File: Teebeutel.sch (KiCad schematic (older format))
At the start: 71 parts, among them J1 RJ45_Shielded, J2 Conn_01x30_Female, J3 Micro_SD_Card, Q1 S8050, Q2 S8050, Q3 S8050, SW1 K1-1506SN-01, U1 ESP32-WROOM-32, U2 TLV1117-33, U3 MCP73831-2-OT, U4 SDB628, U5 LIS2DE12, U6 TLV70018_SOT23-5, U7 SGP30, U8 PPSI262, U9 TXB0104RUT

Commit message: feat: alot of stuff and routing
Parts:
- added C1, C12, C2, C3, C4: 100n, Capacitor_SMD:C_0603_1608Metric, symbol Device:C
- added J3: Battery, Connector_PinHeader_2.54mm:PinHeader_1x02_P2.54mm_Vertical, symbol Connector_Generic:Conn_01x02
- added R20: 30k, Resistor_SMD:R_0603_1608Metric, symbol Device:R
- added R21: 100k, Resistor_SMD:R_0603_1608Metric, symbol Device:R
- added SW2: SW_SPST, Button_Switch_SMD:SW_SPDT_PCM12, symbol Switch:SW_SPDT
- added TP1: ESP32 EN, TestPoint:TestPoint_Pad_D1.0mm, symbol Connector:TestPoint
- added TP10: DTR 3.3V, TestPoint:TestPoint_Pad_D1.0mm, symbol Connector:TestPoint
- added TP11: TxD 3.3V, TestPoint:TestPoint_Pad_D1.0mm, symbol Connector:TestPoint
- added TP12: RxD 3.3V, TestPoint:TestPoint_Pad_D1.0mm, symbol Connector:TestPoint
- added TP13: RTS 3.3V, TestPoint:TestPoint_Pad_D1.0mm, symbol Connector:TestPoint
- added TP14: I²C SDA, TestPoint:TestPoint_Pad_D1.0mm, symbol Connector:TestPoint
- added TP15: I²C SCL, TestPoint:TestPoint_Pad_D1.0mm, symbol Connector:TestPoint
- added TP16, TP17: TestPoint, TestPoint:TestPoint_Pad_D1.0mm, symbol Connector:TestPoint
- added TP18: SD-Card CS, TestPoint:TestPoint_Pad_D1.0mm, symbol Connector:TestPoint
- added TP19: SD-Card MISO, TestPoint:TestPoint_Pad_D1.0mm, symbol Connector:TestPoint
- added TP2: WS2821, TestPoint:TestPoint_Pad_D1.0mm, symbol Connector:TestPoint
- added TP20: SD-Card MOSI, TestPoint:TestPoint_Pad_D1.0mm, symbol Connector:TestPoint
- added TP21: SD-Card SCK, TestPoint:TestPoint_Pad_D1.0mm, symbol Connector:TestPoint
- added TP22: V +5V, TestPoint:TestPoint_Pad_D1.0mm, symbol Connector:TestPoint
- added TP23: V Battery, TestPoint:TestPoint_Pad_D1.0mm, symbol Connector:TestPoint
- added TP24: Charging status, TestPoint:TestPoint_Pad_D1.0mm, symbol Connector:TestPoint
- added TP25: ADC Battery (1/4 Battery voltage), TestPoint:TestPoint_Pad_D1.0mm, symbol Connector:TestPoint
- added TP26: V +1.8V, TestPoint:TestPoint_Pad_D1.0mm, symbol Connector:TestPoint
- added TP27: OLED VPP (13V), TestPoint:TestPoint_Pad_D1.0mm, symbol Connector:TestPoint
- added TP28: OLED SDA, TestPoint:TestPoint_Pad_D1.0mm, symbol Connector:TestPoint
- added TP29: OLED SCK, TestPoint:TestPoint_Pad_D1.0mm, symbol Connector:TestPoint
- added TP3: Button Down, TestPoint:TestPoint_Pad_D1.0mm, symbol Connector:TestPoint
- added TP30: OLED CS, TestPoint:TestPoint_Pad_D1.0mm, symbol Connector:TestPoint
- added TP31: OLED DC, TestPoint:TestPoint_Pad_D1.0mm, symbol Connector:TestPoint
- added TP32: OLED RESET, TestPoint:TestPoint_Pad_D1.0mm, symbol Connector:TestPoint
- added TP33: Touch Button 1, Symbol:OSHW-Symbol_13.4x12mm_Copper, symbol Connector:TestPoint
- added TP34: Touch Button 2, Symbol:OSHW-Symbol_13.4x12mm_Copper, symbol Connector:TestPoint
- added TP35: V +3.3V, TestPoint:TestPoint_Pad_D1.0mm, symbol Connector:TestPoint
- added TP4: Button Left, TestPoint:TestPoint_Pad_D1.0mm, symbol Connector:TestPoint
- added TP5: Button Up, TestPoint:TestPoint_Pad_D1.0mm, symbol Connector:TestPoint
- added TP6: ESP32 IO0, TestPoint:TestPoint_Pad_D1.0mm, symbol Connector:TestPoint
- added TP7: Button Push, TestPoint:TestPoint_Pad_D1.0mm, symbol Connector:TestPoint
- added TP8: Button Right, TestPoint:TestPoint_Pad_D1.0mm, symbol Connector:TestPoint
- added TP9: Buzzer, TestPoint:TestPoint_Pad_D1.0mm, symbol Connector:TestPoint
- BZ1: footprint (none) -> custom_parts:KLJ-5020
- Q1, Q2, Q3: footprint Package_TO_SOT_THT:TO-92_Inline -> Package_TO_SOT_SMD:SOT-23; symbol Transistor_BJT:S8050 -> custom-parts:S8050-J3Y
- gave numbers to parts that had none: 1
- renumbered C2 to C10, C4 to C11, C5 to C13, C6 to C14, C7 to C15, C8 to C16, C9 to C17, C10 to C18, C14 to C19, C3 to C20, C15 to C21, C16 to C22, C11 to C23, C17 to C24, C18 to C5, C19 to C6, C12 to C7, C13 to C8, C1 to C9, D4 to D1, D3 to D10, D7 to D2, D8 to D3, D9 to D4, D10 to D5, D5 to D6, D6 to D7, D1 to D8, D2 to D9, J3 to J2, J2 to J4, R18 to R10, R23 to R11, R8 to R12, R19 to R13, R16 to R14, R20 to R15, R3 to R16, R9 to R18, R10 to R19, R4 to R22, R7 to R23, R5 to R24, R6 to R25, R11 to R3, R12 to R4, R13 to R5, R21 to R6, R22 to R7, R14 to R8, R15 to R9, U2 to U10, U9 to U3, U5 to U4, U7 to U5, U8 to U6, U3 to U7, U6 to U8, U4 to U9
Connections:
- net labels added: ADC-BAT
- wire segments 238 -> 294
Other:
- moved on the sheet: C10, C11, C13, C14, C15, C16, C17, C18, C19, C20, C21, C22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

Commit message: feat: alot of stuff
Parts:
- removed BZ1: Buzzer, custom_parts:KLJ-5020, symbol Device:Buzzer
- removed D2, D3, D4: WS2812B, LED_SMD:LED_WS2812B_PLCC4_5.0x5.0mm_P3.2mm, symbol LED:WS2812B
- removed D5: SM4007, Diode_SMD:D_SOD-123, symbol Diode:SM4007
- removed Q3: S8050, Package_TO_SOT_SMD:SOT-23, symbol custom-parts:S8050-J3Y
- removed TP22: V +5V, TestPoint:TestPoint_Pad_D1.0mm, symbol Connector:TestPoint
- removed TP23: V Battery, TestPoint:TestPoint_Pad_D1.0mm, symbol Connector:TestPoint
- removed TP33: Touch Button 1, Symbol:OSHW-Symbol_13.4x12mm_Copper, symbol Connector:TestPoint
- removed TP9: Buzzer, TestPoint:TestPoint_Pad_D1.0mm, symbol Connector:TestPoint
- added C1, C11, C12, C13, C14, C4, C7, C9: 100n, Capacitor_SMD:C_0603_1608Metric, symbol Device:C
- added D1, D10, D11, D12, D3, D4, D5, D6, D7, D8, D9: WS2812B, Teebeutel_Special_Parts:WS2812B-4020, symbol Teebeutel_Special_Parts:WS2812B-4020
- added TB1: Touch Button 2, Teebeutel_Graphics:Touch-Button_Python, symbol Connector:TestPoint
- D13: renamed from D6; value LED -> LED-RED
- D14: renamed from D7; value LED -> LED-GREEN
- D2: renamed from D1; footprint LED_SMD:LED_WS2812B_PLCC4_5.0x5.0mm_P3.2mm -> Teebeutel_Special_Parts:WS2812B-4020; symbol LED:WS2812B -> Teebeutel_Special_Parts:WS2812B-4020; JLCPCB C139127 -> C965557
- J2: footprint custom_parts:TF15X15 -> Teebeutel_Special_Parts:TF15X15
- Q1, Q2: symbol custom-parts:S8050-J3Y -> Teebeutel_Special_Parts:S8050-J3Y
- R11: value 180 -> 10k
- R20: value 30k -> 300k
- SW1: footprint custom_parts:K1-1506SN-01 -> Teebeutel_Special_Parts:K1-1506SN-01; symbol custom-parts:K1-1506SN-01 -> Teebeutel_Special_Parts:K1-1506SN-01
- TB2: renamed from TP34; footprint Symbol:OSHW-Symbol_13.4x12mm_Copper -> Teebeutel_Graphics:Touch-Button_OSHW
- U5: footprint custom_parts:SGP30 -> Teebeutel_Special_Parts:SGP30; symbol custom-parts:SGP30 -> Teebeutel_Special_Parts:SGP30
- U6: footprint custom_parts:PPSI262 -> Teebeutel_Special_Parts:PPSI262; symbol custom-parts:PPSI262 -> Teebeutel_Special_Parts:PPSI262
- U9: symbol custom-parts:SDB628 -> Teebeutel_Special_Parts:SDB628
- renumbered C4 to C10, C5 to C15, C6 to C16, C9 to C17, C10 to C18, C11 to C19, C1 to C2, C12 to C20, C13 to C21, C14 to C22, C15 to C23, C16 to C24, C17 to C25, C18 to C26, C19 to C27, C20 to C28, C21 to C29, C7 to C3, C22 to C30, C23 to C31, C24 to C32, C2 to C5, C8 to C6, C3 to C8, D8 to D15, D9 to D16, D10 to D17, R12 to R1, R8 to R10, R9 to R12, R1 to R2, R2 to R3, R6 to R4, R7 to R5, R3 to R6, R10 to R7, R4 to R8, R5 to R9, TP12 to TP10, TP13 to TP11, TP8 to TP12, TP14 to TP13, TP15 to TP14, TP16 to TP15, TP17 to TP16, TP18 to TP17, TP19 to TP18, TP20 to TP19, TP21 to TP20, TP24 to TP21, TP25 to TP22, TP26 to TP23, TP27 to TP24, TP28 to TP25, TP29 to TP26, TP30 to TP27, TP31 to TP28, TP32 to TP29, TP6 to TP3, TP35 to TP30, TP3 to TP4, TP4 to TP5, TP5 to TP6, TP10 to TP8, TP11 to TP9, U4 to U1, U1 to U2, U2 to U3, U3 to U4
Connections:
- net labels removed: BUZZER
- wire segments 294 -> 315
- no-connect marks 23 -> 29
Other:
- moved on the sheet: C10, C2, C3, C5, C6, C8, R1, R10, R12, R6, R8, R9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

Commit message: feat(): Finished routing and some clean up
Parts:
- added R26: 10, Resistor_SMD:R_0603_1608Metric, symbol Device:R
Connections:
- net SD-SCK: now also R26.2; no longer J2.5 (CLK), TP20.1
- new net: J2.5 (CLK), R26.1, TP20.1
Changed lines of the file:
@@
 Text GLabel 8750 1650 0    50   Input ~ 0
 SD-MISO
-Text GLabel 8750 1250 0    50   Input ~ 0
+Text GLabel 8450 1250 1    50   Input ~ 0
 SD-MOSI
-Text GLabel 8750 1150 0    50   Input ~ 0
-SD-CS
-Text GLabel 8750 1450 0    50   Input ~ 0
+Text GLabel 8450 1450 0    50   Input ~ 0
 SD-SCK
 $Comp
@@
 Wire Wire Line
 	8750 1150 9000 1150
-Wire Wire Line
-	8750 1250 8950 1250
 $Comp
 L Connector:TestPoint TP19
@@
 NoConn ~ 7000 10500
 NoConn ~ 12000 7250
+$Comp
+L Device:R R26
+U 1 1 6238B3D1
+P 8600 1450
+F 0 "R26" H 8530 1404 50  0000 R CNN
+F 1 "10" H 8530 1495 50  0000 R CNN
+F 2 "Resistor_SMD:R_0603_1608Metric" V 8530 1450 50  0001 C CNN
+F 3 "~" H 8600 1450 50  0001 C CNN
+	1    8600 1450
+	0    1    1    0
+$EndComp
+Text GLabel 8600 1150 1    50   Input ~ 0
+SD-CS
+Wire Wire Line
+	8600 1150 8750 1150
+Connection ~ 8750 1150
+Wire Wire Line
+	8450 1250 8950 1250
 $EndSCHEMATC

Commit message: feat(): finish routing and assigning JLCPCB part numbers
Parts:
- added R27, R28: 100, Resistor_SMD:R_0603_1608Metric, symbol Device:R
- C1, C10, C11, C12, C13, C14, C15, C16, C2, C20, C24, C27, C3, C30, C4, C5, C7, C8, C9: JLC (none) -> 0603; LCSC (none) -> C14663
- C17, C18, C21, C23, C29, C32, C6: JLC (none) -> 0603; LCSC (none) -> C19702
- C19, C22: JLC (none) -> 0603; LCSC (none) -> C15849
- C25, C26: JLC (none) -> 0603; LCSC (none) -> C19666
- C28, C31: JLC (none) -> 0603; LCSC (none) -> C59461
- D1, D10, D11, D12, D2, D3, D4, D5, D6, D7, D8, D9: JLC (none) -> 4.0x2.0mm; JLCPCB C965557 -> (none); LCSC (none) -> C965557
- D13: footprint LED_SMD:LED_1210_3225Metric -> LED_SMD:LED_0805_2012Metric; JLC (none) -> LED_0805; LCSC (none) -> C84256
- D14: footprint LED_SMD:LED_1210_3225Metric -> LED_SMD:LED_0805_2012Metric; JLC (none) -> LED_0805; LCSC (none) -> C2297
- D15, D16: JLC (none) -> SOD-523; LCSC (none) -> C393518
- D17: JLC (none) -> DO-214AC; JLCPCB C2480 -> (none); LCSC (none) -> C2480
- J1: footprint Connector_RJ:RJ45_Amphenol_RJHSE5380 -> Connector_RJ:RJ45_Amphenol_RJHSE538X; symbol Connector:RJ45_Shielded -> Connector:RJ45_LED_Shielded; JLC (none) -> RJ45-TH; LCSC (none) -> C464587
- J2: JLC (none) -> 14.5x14.75x1.85mm; JLCPCB C266621 -> (none); LCSC (none) -> C266621
- J4: JLC (none) -> SMD; JLCPCB C2856808 -> (none); LCSC (none) -> C2856808
- L1: JLC (none) -> 1210; JLCPCB C86070 -> (none); LCSC (none) -> C86070
- Q1, Q2: JLC (none) -> SOT-23-3; JLCPCB C2146 -> (none); LCSC (none) -> C2146
- R1, R10, R11, R12, R13, R14, R15, R17, R2, R3, R4, R5, R6, R7, R8, R9: JLC (none) -> 0603; LCSC (none) -> C25804
- R16: JLC (none) -> R0603; LCSC (none) -> C113303
- R18, R19: JLC (none) -> R0603; LCSC (none) -> C116694
- R20: JLC (none) -> 0603; LCSC (none) -> C23024
- R21: JLC (none) -> 0603; LCSC (none) -> C25803
- R22: value 50 -> 56; JLC (none) -> 0603; LCSC (none) -> C25196
- R23: JLC (none) -> 0603; LCSC (none) -> C23203
- R24: JLC (none) -> 0603; LCSC (none) -> C23219
- R25: JLC (none) -> 0603; LCSC (none) -> C22984
- R26: JLC (none) -> 0603; LCSC (none) -> C22859
- SW1: JLC (none) -> KEY-SMD; JLCPCB C145910 -> (none); LCSC (none) -> C145910
- SW2: JLC (none) -> SW-SMD; JLCPCB C319020 -> (none); LCSC (none) -> C319020
- TP15: value TestPoint -> I²C SDA 1.8V
- TP16: value TestPoint -> I²C SCL 1.8V
- U1: JLC (none) -> LGA-12_2.0x2.0x0.5P; JLCPCB C189624 -> (none); LCSC (none) -> C189624
- U10: JLC (none) -> SOT-223; JLCPCB C15578 -> (none); LCSC (none) -> C15578
- U2: JLC (none) -> QFN-38_EP_18.0x25.0x1.27P; JLCPCB C82899 -> (none); LCSC (none) -> C82899
- U3, U4: JLC (none) -> UQFN-12_1.7x2.0x0.4P; JLCPCB C105266 -> (none); LCSC (none) -> C105266
- U5: JLC (none) -> DFN-6_EP_2.5x2.5x0.8P; JLCPCB C514454 -> (none); LCSC (none) -> C514454
- U6: JLC (none) -> SENSOR-SMD; JLCPCB C328758 -> (none); LCSC (none) -> C328758
- U7: JLC (none) -> SOT-23-5; JLCPCB C14879 -> (none); LCSC (none) -> C14879
- U8: JLC (none) -> SOT-23-5; JLCPCB C79924 -> (none); LCSC (none) -> C79924
- U9: JLC (none) -> SOT-23-6L; JLCPCB C77805 -> (none); LCSC (none) -> C77805
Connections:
- net GND: now also J1.11, J1.9
- net RxD: now also R28.1
- net TxD: now also R27.1
- new net: J1.10, R28.2
- new net: J1.12, R27.2

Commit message: feat(): add IR-Tranceiver and some 3D-Models
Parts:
- added D9: LED-IR, Teebeutel_Special_Parts:LKIR30102C, symbol Device:LED
- added R6: 82, Resistor_SMD:R_0603_1608Metric, symbol Device:R
- added TP4: IR-TX, TestPoint:TestPoint_Pad_D1.0mm, symbol Connector:TestPoint
- added TP8: IR-RX, TestPoint:TestPoint_Pad_D1.0mm, symbol Connector:TestPoint
- added U3: RM-V8xxC_TR1, Teebeutel_Special_Parts:IRM-V8xxC-TR1, symbol Teebeutel_Special_Parts:RM-V8xxC_TR1
- renumbered D9 to D10, D10 to D11, D11 to D12, D12 to D13, D13 to D14, D14 to D15, D15 to D16, D16 to D17, D17 to D18, R8 to R10, R9 to R11, R28 to R12, R10 to R13, R11 to R14, R12 to R15, R13 to R16, R14 to R17, R15 to R18, R26 to R19, R16 to R20, R17 to R21, R18 to R22, R19 to R23, R20 to R24, R21 to R25, R22 to R26, R23 to R27, R24 to R28, R25 to R29, R6 to R7, R27 to R8, R7 to R9, TP8 to TP10, TP9 to TP11, TP10 to TP12, TP11 to TP13, TP12 to TP14, TP13 to TP15, TP14 to TP16, TP15 to TP17, TP16 to TP18, TP17 to TP19, TP18 to TP20, TP19 to TP21, TP20 to TP22, TP21 to TP23, TP22 to TP24, TP23 to TP25, TP24 to TP26, TP25 to TP27, TP26 to TP28, TP27 to TP29, TP28 to TP30, TP29 to TP31, TP30 to TP32, TP4 to TP5, TP5 to TP6, TP6 to TP7, TP7 to TP9, U9 to U10, U10 to U11, U3 to U4, U4 to U5, U5 to U6, U6 to U7, U7 to U8, U8 to U9
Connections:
- net +3V3: now also U3.2 (VCC)
- net GND: now also D9.1 (K), U3.1 (GND), U3.4 (GND)
- net IR-TX: now reaches U2.37 (IO23)
- net IR-TX: now also R6.2, TP4.1
- net IR-RX: now reaches U2.5 (SENSOR_VN)
- net IR-RX: now also TP8.1, U3.3 (OUT)
- new net: D9.2 (A), R6.1

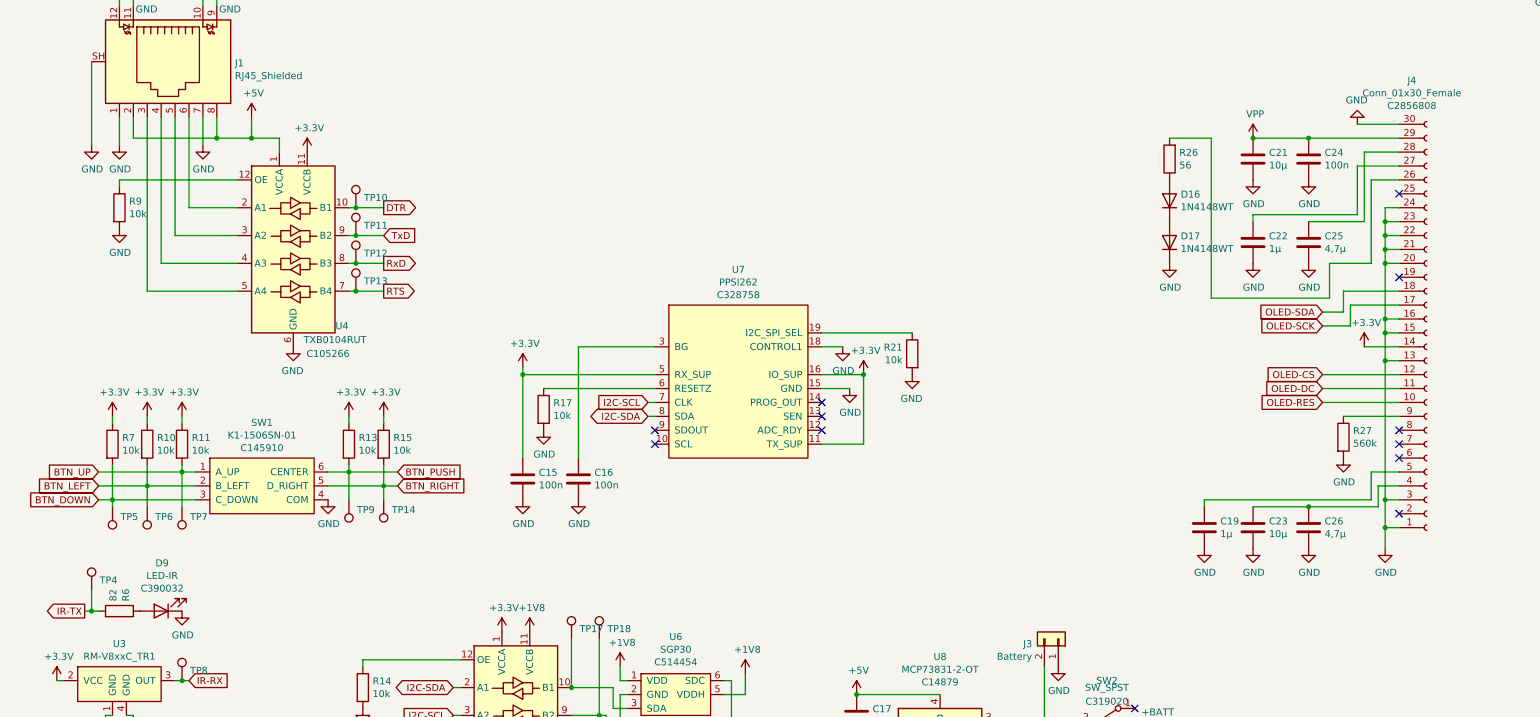
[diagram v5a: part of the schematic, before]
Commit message: fix: use the correct display connector
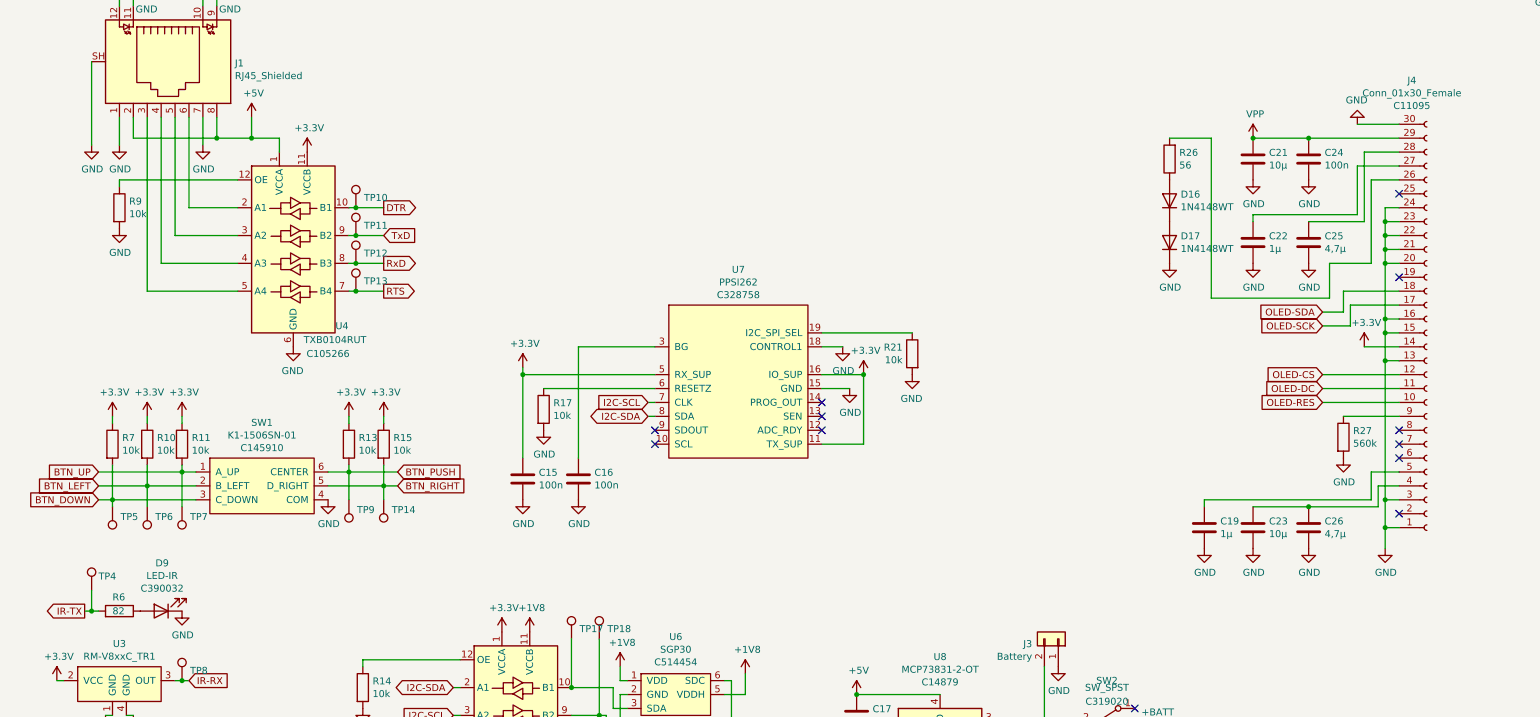
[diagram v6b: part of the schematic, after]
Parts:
- J4: footprint Connector_FFC-FPC:TE_3-84953-0_1x30-1MP_P1.0mm_Horizontal -> Connector_FFC-FPC:TE_3-1734839-0_1x30-1MP_P0.5mm_Horizontal; JLC SMD -> 30P; LCSC C2856808 -> C11095
- R6: LCSC C25804 -> C4275
- TB1: value Touch Button 2 -> Touch Button 1
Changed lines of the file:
@@
 F 0 "J4" H 13992 2735 50  0000 C CNN
 F 1 "Conn_01x30_Female" H 13992 2826 50  0000 C CNN
-F 2 "Connector_FFC-FPC:TE_3-84953-0_1x30-1MP_P1.0mm_Horizontal" H 14100 4550 50  0001 C CNN
-F 3 "~" H 14100 4550 50  0001 C CNN
-F 4 "C2856808" H 13992 2917 50  0000 C CNN "LCSC"
-F 5 "SMD" H 14100 4550 50  0001 C CNN "JLC"
+F 2 "Connector_FFC-FPC:TE_3-1734839-0_1x30-1MP_P0.5mm_Horizontal" H 14100 4550 50  0001 C CNN
+F 3 "https://datasheet.lcsc.com/lcsc/1811021327_JUSHUO-AFC07-S30ECC-00_C11095.pdf" H 14100 4550 50  0001 C CNN
+F 4 "C11095" H 13992 2917 50  0000 C CNN "LCSC"
+F 5 "30P" H 14100 4550 50  0001 C CNN "JLC"
 	1    14100 4550
 	1    0    0    1
@@
 P 15550 3250
 F 0 "TB1" V 15550 3438 50  0000 L CNN
-F 1 "Touch Button 2" H 15608 3277 50  0001 L CNN
+F 1 "Touch Button 1" H 15608 3277 50  0001 L CNN
 F 2 "Teebeutel_Graphics:Touch-Button_Python" H 15750 3250 50  0001 C CNN
 F 3 "~" H 15750 3250 50  0001 C CNN
@@
 U 1 1 61A2C983
 P 4700 6550
-F 0 "R6" H 4770 6596 50  0000 L CNN
-F 1 "82" H 4770 6505 50  0000 L CNN
+F 0 "R6" V 4800 6500 50  0000 L CNN
+F 1 "82" V 4700 6500 50  0000 L CNN
 F 2 "Resistor_SMD:R_0603_1608Metric" V 4630 6550 50  0001 C CNN
 F 3 "~" H 4700 6550 50  0001 C CNN
 F 4 "0603" H 4700 6550 50  0001 C CNN "JLC"
-F 5 "C25804" H 4700 6550 50  0001 C CNN "LCSC"
+F 5 "C4275" V 4600 6550 50  0001 C CNN "LCSC"
 	1    4700 6550
 	0    1    -1   0
@@
 U 1 1 61A727F6
 P 4500 6400
-F 0 "TP4" H 4558 6472 50  0000 L CNN
+F 0 "TP4" H 4550 6500 50  0000 L CNN
 F 1 "IR-TX" H 4558 6427 50  0001 L CNN
 F 2 "TestPoint:TestPoint_Pad_D1.0mm" H 4700 6400 50  0001 C CNN
